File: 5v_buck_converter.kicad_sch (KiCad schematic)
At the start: 0 parts

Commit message: Finished 5V buck converter schematic
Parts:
- added C15, C20, C22: 22uF, symbol Device:C
- added C16, C17, C21: 10uF, symbol Device:C
- added C18: 0.1uF, symbol Device:C
- added C19: 0.1uF, symbol Device:C_Small
- added IC2: TPS62933ODRLR, SOTFL50P160X60-8N, symbol utsvt-chips:TPS62933ODRLR
- added L2: 6.6uH, symbol Device:L
- added Q6: BUK9K52-60RAX, symbol Device:Q_Dual_NMOS_S1G1S2G2D2D2D1D1
- added R27: 1.5k, symbol Device:R_Small
- added R28: 10k, symbol Device:R_Small
- added R30: 51k, symbol Device:R_Small
- added R31: 200k, symbol Device:R_Small
- added R33: 18k, symbol Device:R_Small
- added R34: 360, symbol Device:R_Small
- added R35: 10k, symbol Device:R
- added R36: 1k, symbol Device:R
- added R4: 5, symbol Device:R_Small
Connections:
- new net: IC2.2 (EN), R31.2, R33.1
- new net: R33.2, R34.1
- new net: Q6.2 (G), Q6.4 (G), R35.2, R36.2
- new net: C19.1, IC2.5 (SW), L2.1
- new net: C19.2, R4.2
- new net: IC2.6 (BST), R4.1
- new net: R27.1, R30.2
- new net: IC2.8 (FB), R27.2, R28.1
- new net: Q6.1 (S), Q6.3 (S)
- new net +3.3V: R35.1
- new net 5V_OUT: Q6.5 (D), Q6.6 (D)
- new net GND: C15.1, C16.2, C17.2, C18.2, C20.1, C21.1, C22.1, IC2.4 (GND), R28.2, R34.2
- new net POWER_GOOD: IC2.7 (PG), R36.1
- new net VBUS_IN: C16.1, C17.1, C18.1, IC2.3 (VIN), R31.1
- new net VOUT: C15.2, C20.2, C21.2, C22.2, L2.2, Q6.7 (D), Q6.8 (D), R30.1
- no-connect marks 0 -> 1
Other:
- note added: "3.3V from internal regulator of PD controller"
- note added: "500kHz See datasheet pg. 20"
- note added: "5V Buck"
- note added: "Note: test performance of this output filter to ensure capacitance is not too high. Remove capacitors if necessary."
- note added: "Output MOSFET (N-Channel)"
- note added: "Output Voltage = 5V See datasheet pg. 19"
- note added: "Undervoltage Lockout Settings: Vstart = 14.25V Vstop = 13.5V See datasheet pg. 21"
- company: (none) -> Longhorn Racing Solar

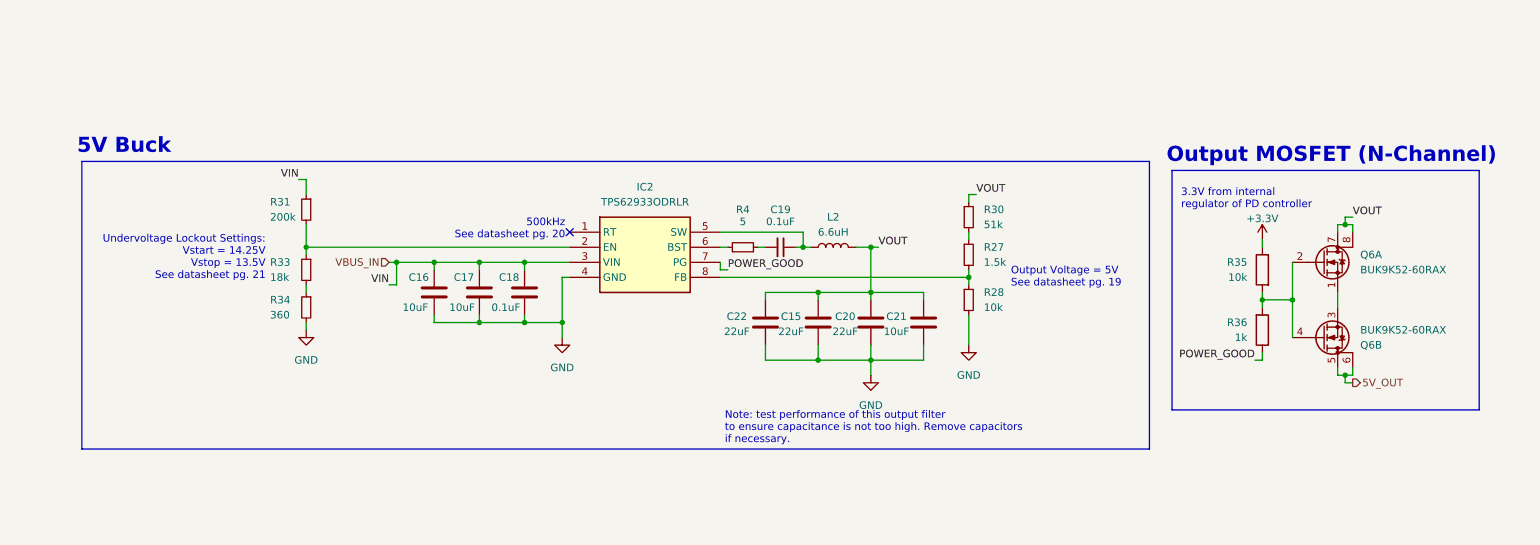
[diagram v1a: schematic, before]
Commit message: added power good LED indicators
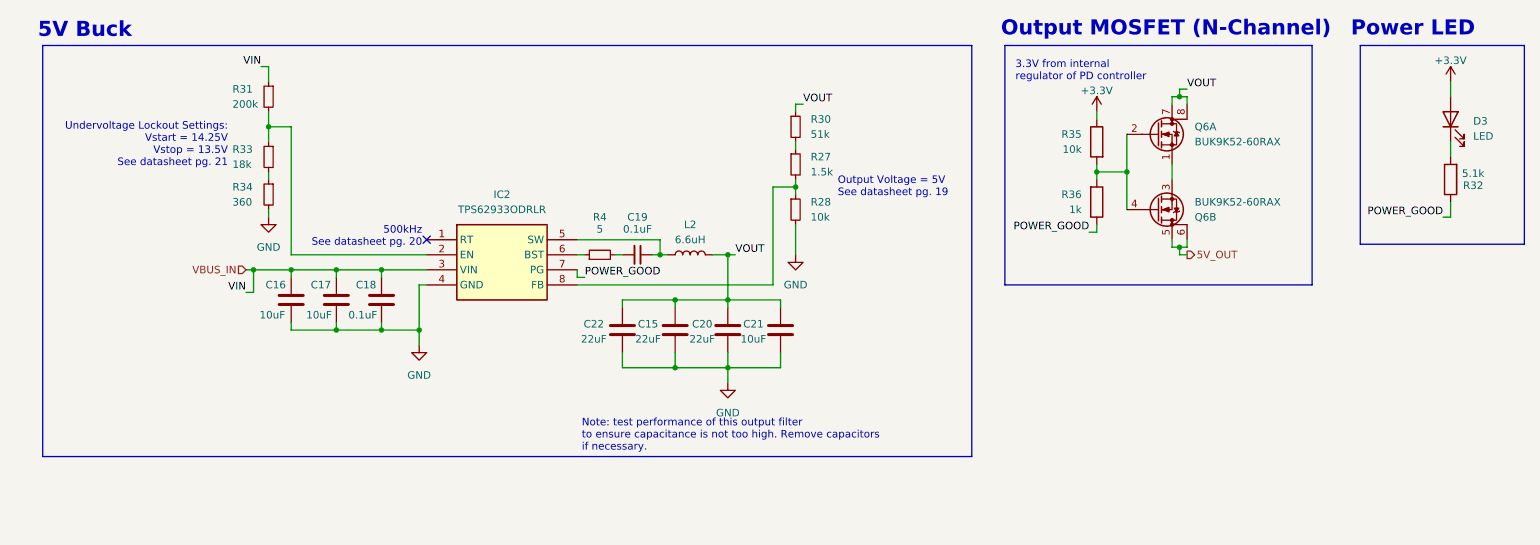
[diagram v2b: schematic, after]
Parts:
- added D3: LED, symbol Device:LED
- added R32: 5.1k, symbol Device:R
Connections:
- net +3.3V: now also D3.2 (A)
- net POWER_GOOD: now also R32.1
- new net: D3.1 (K), R32.2
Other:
- note added: "Power LED"
- moved on the sheet: C15, C16, C17, C18, C19, C20, C21, C22, IC2, L2, Q6A, Q6B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

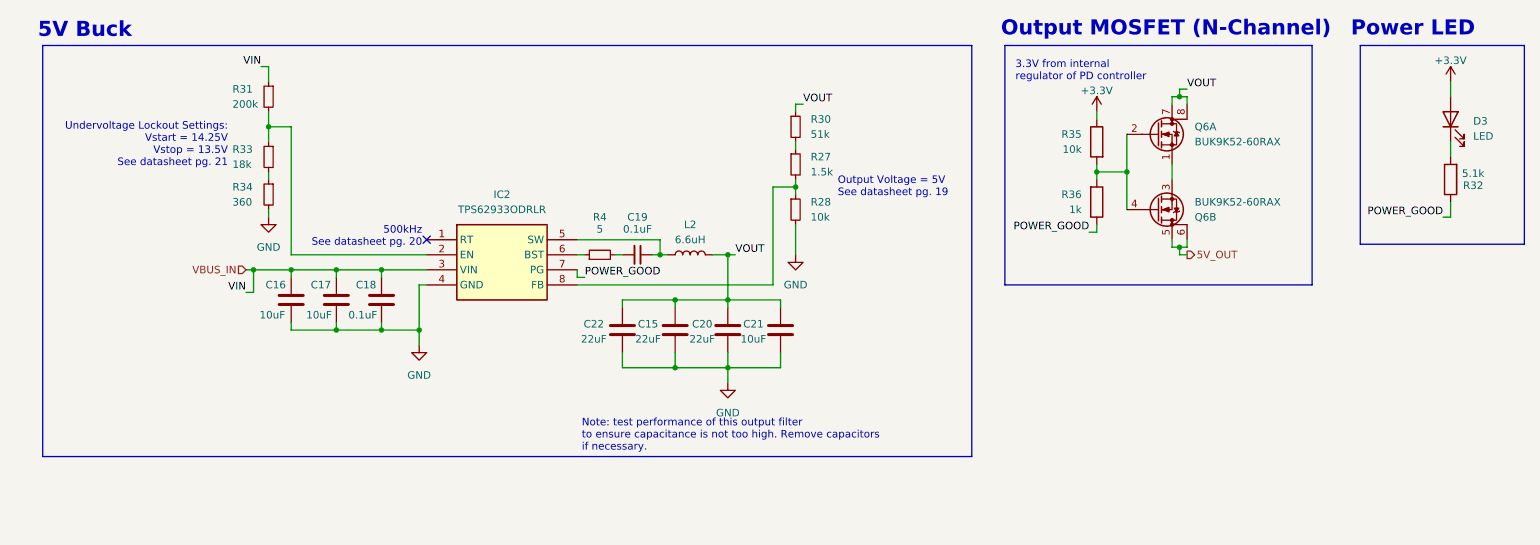
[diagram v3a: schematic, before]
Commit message: updated with some new footprints (have yet to finish footprint assignment; also need to switch out inductor for 5V buck)
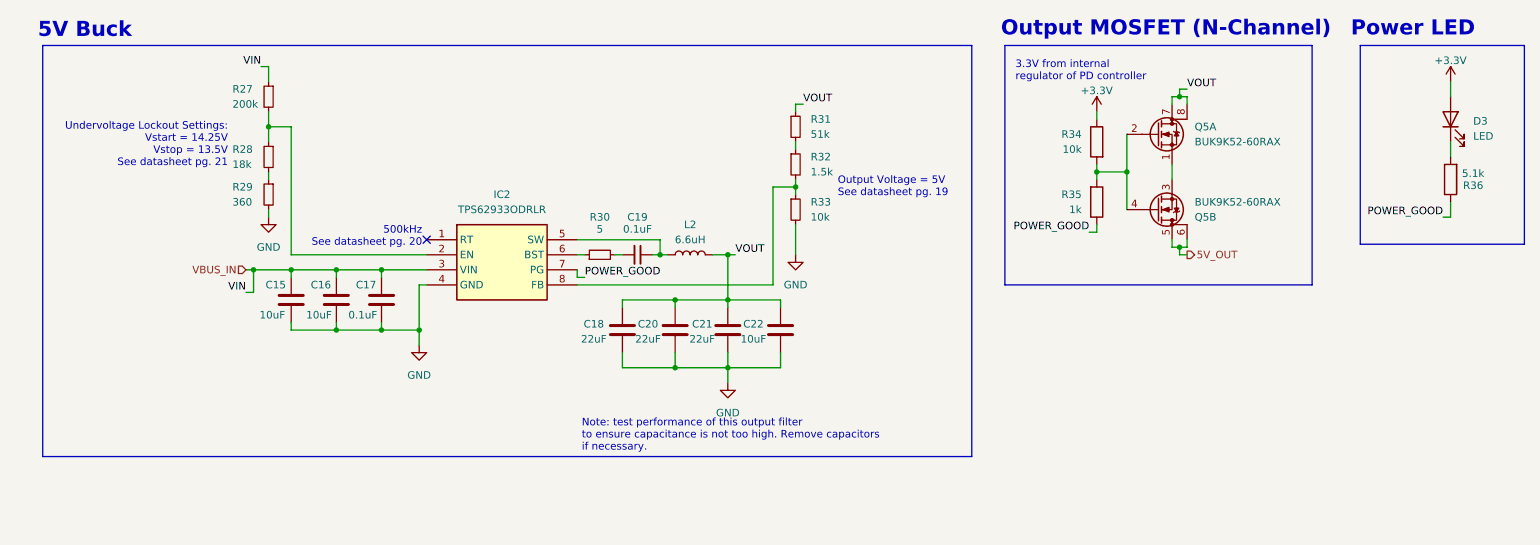
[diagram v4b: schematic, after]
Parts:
- C15: renamed from C16; footprint (none) -> Capacitor_SMD:C_0805_2012Metric
- C16: renamed from C17; footprint (none) -> Capacitor_SMD:C_0805_2012Metric
- C17: renamed from C18; footprint (none) -> Capacitor_SMD:C_0805_2012Metric
- C18: renamed from C22; footprint (none) -> Capacitor_SMD:C_0805_2012Metric
- C19: footprint (none) -> Capacitor_SMD:C_0805_2012Metric
- C20: renamed from C15; footprint (none) -> Capacitor_SMD:C_0805_2012Metric
- C21: renamed from C20; footprint (none) -> Capacitor_SMD:C_0805_2012Metric
- C22: renamed from C21; footprint (none) -> Capacitor_SMD:C_0805_2012Metric
- IC2: footprint SOTFL50P160X60-8N -> UTSVT_Power:SOTFL50P160X60-8N; symbol utsvt-chips:TPS62933ODRLR -> utsvt-power-regulators:TPS62933ODRLR
- R27: renamed from R31; footprint (none) -> Resistor_SMD:R_0805_2012Metric
- R28: renamed from R33; footprint (none) -> Resistor_SMD:R_0805_2012Metric
- R29: renamed from R34; footprint (none) -> Resistor_SMD:R_0805_2012Metric
- R30: renamed from R4; footprint (none) -> Resistor_SMD:R_0805_2012Metric
- R31: renamed from R30; footprint (none) -> Resistor_SMD:R_0805_2012Metric
- R32: renamed from R27; footprint (none) -> Resistor_SMD:R_0805_2012Metric
- R33: renamed from R28; footprint (none) -> Resistor_SMD:R_0805_2012Metric
- R34: renamed from R35; footprint (none) -> Resistor_SMD:R_0805_2012Metric
- R35: renamed from R36; footprint (none) -> Resistor_SMD:R_0805_2012Metric
- R36: renamed from R32; footprint (none) -> Resistor_SMD:R_0805_2012Metric
- renumbered Q6 to Q5

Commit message: changed 5v buck to TPS56A37
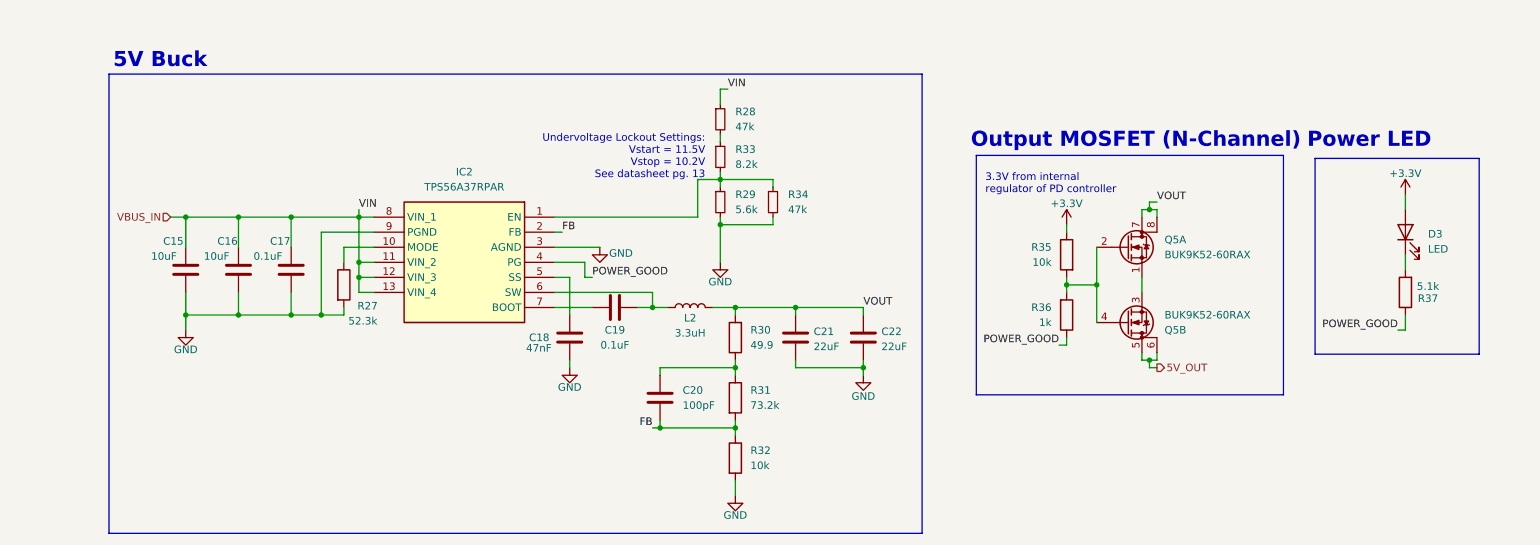
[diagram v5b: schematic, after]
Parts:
- removed C19: 0.1uF, Capacitor_SMD:C_0805_2012Metric, symbol Device:C_Small
- removed IC2: TPS62933ODRLR, UTSVT_Power:SOTFL50P160X60-8N, symbol utsvt-power-regulators:TPS62933ODRLR
- removed R27: 200k, Resistor_SMD:R_0805_2012Metric, symbol Device:R_Small
- removed R30: 5, Resistor_SMD:R_0805_2012Metric, symbol Device:R_Small
- removed R31: 51k, Resistor_SMD:R_0805_2012Metric, symbol Device:R_Small
- removed R32: 1.5k, Resistor_SMD:R_0805_2012Metric, symbol Device:R_Small
- removed R34: 10k, Resistor_SMD:R_0805_2012Metric, symbol Device:R
- added C19: 0.1uF, Capacitor_SMD:C_0805_2012Metric, symbol Device:C
- added IC2: TPS56A37RPAR, UTSVT_Power:TPS56A37RPAR, symbol utsvt-power-regulators:TPS56A37RPAR
- added R27: 52.3k, Resistor_SMD:R_0805_2012Metric, symbol Device:R
- added R30: 49.9, Resistor_SMD:R_0805_2012Metric, symbol Device:R
- added R31: 73.2k, Resistor_SMD:R_0805_2012Metric, symbol Device:R
- added R32: 10k, Resistor_SMD:R_0805_2012Metric, symbol Device:R
- added R34: 47k, Resistor_SMD:R_0805_2012Metric, symbol Device:R_Small
- added R37: 5.1k, Resistor_SMD:R_0805_2012Metric, symbol Device:R
- C18: value 22uF -> 47nF
- C20: value 22uF -> 100pF
- C22: value 10uF -> 22uF
- L2: value 6.6uH -> 3.3uH; footprint (none) -> UTSVT_Passive:INDPM135125X640N; Mouser Part Number (none) -> SRP1265A-5R6M
- R28: value 18k -> 47k
- R29: value 360 -> 5.6k
- R33: value 10k -> 8.2k
- R35: value 1k -> 10k
- R36: value 5.1k -> 1k
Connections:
- net +3.3V: now also R35.1
- net GND: now also C18.2, C21.2, C22.2, IC2.3 (AGND), IC2.9 (PGND), R27.2, R32.2, R34.2; no longer C18.1, C20.1, C21.1, C22.1, R33.2
- net POWER_GOOD: now also IC2.4 (PG), R37.1; no longer R35.1
- net VBUS_IN: now also R28.1, IC2.11 (VIN_2), IC2.12 (VIN_3), IC2.13 (VIN_4), IC2.8 (VIN_1)
- net VOUT: now also C21.1, C22.1, R30.2; no longer C18.2, C20.2, C21.2, C22.2
- net at R28.2: now also R33.1; no longer R29.1
- net at Q5.2 (G), Q5.4 (G), R35.2: now also R36.2
- net at L2.1: now also C19.2, IC2.6 (SW)
- net at D3.1 (K): now also R37.2; no longer R36.2
- new net: C18.1, IC2.5 (SS)
- new net: C20.1, R30.1, R31.1
- new net: IC2.10 (MODE), R27.1
- new net: IC2.1 (EN), R29.1, R33.2, R34.1
- new net: C19.1, IC2.7 (BOOT)
- new net FB: C20.2, IC2.2 (FB), R31.2, R32.1
- no-connect marks 1 -> 0
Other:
- note added: "Undervoltage Lockout Settings: Vstart = 11.5V Vstop = 10.2V See datasheet pg. 13"
- note removed: "500kHz See datasheet pg. 20"
- note removed: "Note: test performance of this output filter to ensure capacitance is not too high. Remove capacitors if necessary."
- note removed: "Output Voltage = 5V See datasheet pg. 19"
- note removed: "Undervoltage Lockout Settings: Vstart = 14.25V Vstop = 13.5V See datasheet pg. 21"

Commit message: almost done w/ schematic, just need to finish footprint assignment (make sure buck converter components are correctly chosen and there aren't caps that need to be different and stuff)
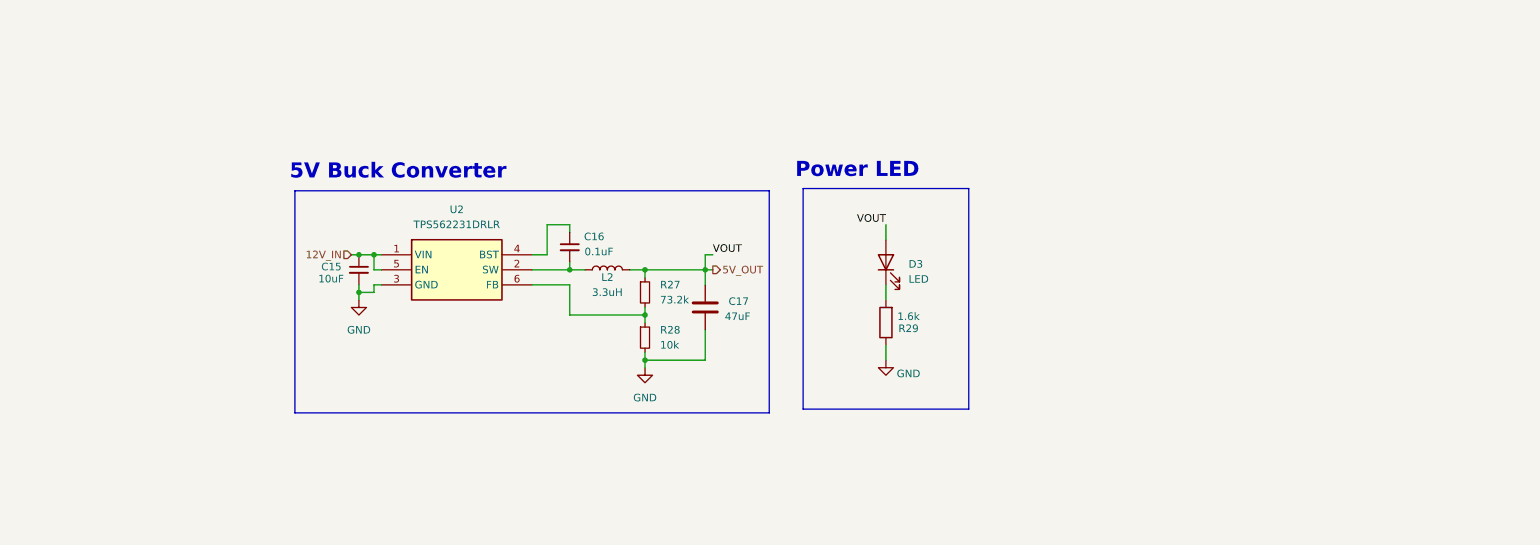
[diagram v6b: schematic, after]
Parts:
- removed C15, C16: 10uF, Capacitor_SMD:C_0805_2012Metric, symbol Device:C
- removed C18: 47nF, Capacitor_SMD:C_0805_2012Metric, symbol Device:C
- removed C19: 0.1uF, Capacitor_SMD:C_0805_2012Metric, symbol Device:C
- removed C20: 100pF, Capacitor_SMD:C_0805_2012Metric, symbol Device:C
- removed C21, C22: 22uF, Capacitor_SMD:C_0805_2012Metric, symbol Device:C
- removed IC2: TPS56A37RPAR, UTSVT_Power:TPS56A37RPAR, symbol utsvt-power-regulators:TPS56A37RPAR
- removed Q5: BUK9K52-60RAX, symbol Device:Q_Dual_NMOS_S1G1S2G2D2D2D1D1
- removed R27: 52.3k, Resistor_SMD:R_0805_2012Metric, symbol Device:R
- removed R29: 5.6k, Resistor_SMD:R_0805_2012Metric, symbol Device:R_Small
- removed R30: 49.9, Resistor_SMD:R_0805_2012Metric, symbol Device:R
- removed R31: 73.2k, Resistor_SMD:R_0805_2012Metric, symbol Device:R
- removed R32, R35: 10k, Resistor_SMD:R_0805_2012Metric, symbol Device:R
- removed R33: 8.2k, Resistor_SMD:R_0805_2012Metric, symbol Device:R_Small
- removed R34: 47k, Resistor_SMD:R_0805_2012Metric, symbol Device:R_Small
- removed R36: 1k, Resistor_SMD:R_0805_2012Metric, symbol Device:R
- added C15: 10uF, Capacitor_SMD:C_0805_2012Metric, symbol Device:C_Small
- added C16: 0.1uF, Capacitor_SMD:C_0805_2012Metric, symbol Device:C_Small
- added R27: 73.2k, symbol Device:R_Small
- added U2: TPS562231DRLR, Package_TO_SOT_SMD:SOT-563, symbol utsvt-power-regulators:TPS562231DRLR
- C17: value 0.1uF -> 47uF
- D3: footprint (none) -> LED_SMD:LED_0805_2012Metric; Mouser Part Number (none) -> APTD2012LCGCK
- L2: footprint UTSVT_Passive:INDPM135125X640N -> (none); Mouser Part Number SRP1265A-5R6M -> LBC3225T3R3MR
- R28: value 47k -> 10k; footprint Resistor_SMD:R_0805_2012Metric -> (none)
- R29: renamed from R37; value 5.1k -> 1.6k
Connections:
- net +3.3V is gone; now on net 5V_OUT: D3.2 (A)
- net POWER_GOOD is gone; now on net GND: R29.1
- net VOUT is gone; now on net 5V_OUT: L2.2
- net 5V_OUT: now also C17.1, R27.1
- net GND: now also R28.2, C15.2, U2.3 (GND)
- net at L2.1: now also C16.2, U2.2 (SW)
- net VBUS_IN: no longer names the net of R28.1
- net VBUS_IN: now also R27.2, U2.6 (FB); no longer C17.1
- new net: C16.1, U2.4 (BST)
- new net 12V_IN: C15.1, U2.1 (VIN), U2.5 (EN)
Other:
- note added: "5V Buck Converter"
- note removed: "3.3V from internal regulator of PD controller"
- note removed: "5V Buck"
- note removed: "Output MOSFET (N-Channel)"
- note removed: "Undervoltage Lockout Settings: Vstart = 11.5V Vstop = 10.2V See datasheet pg. 13"
- moved on the sheet: D3, R29

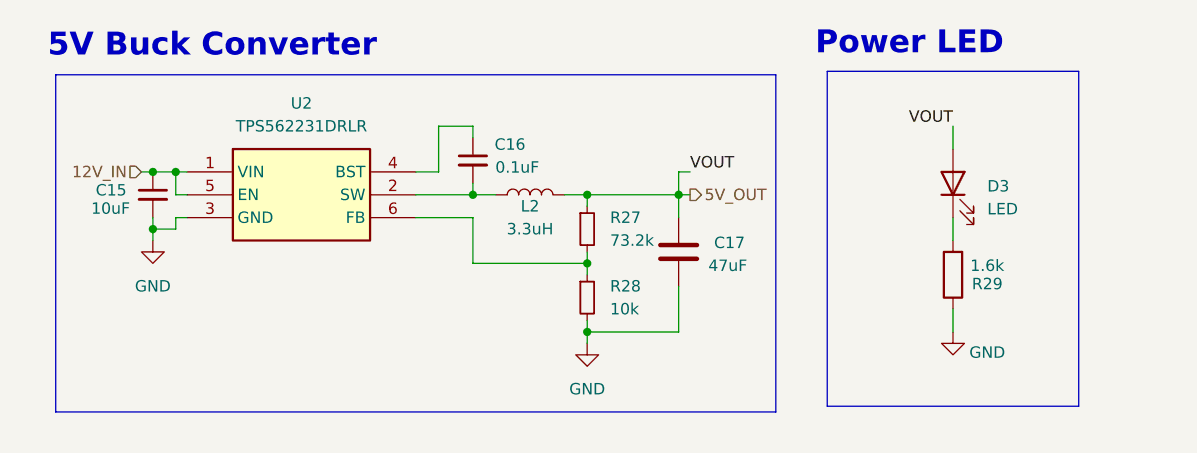
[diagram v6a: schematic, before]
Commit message: cleaned up schematic, added power LEDs and testpoints
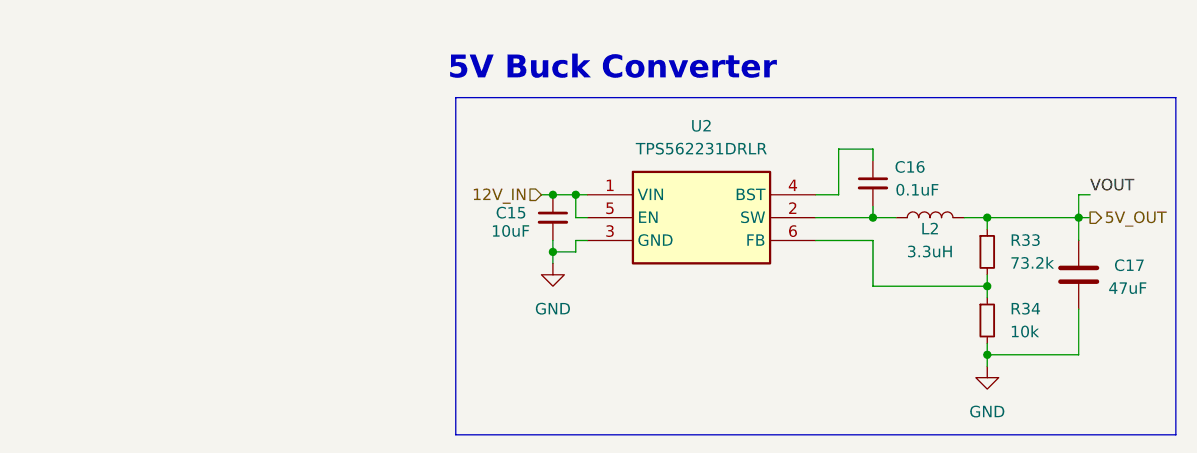
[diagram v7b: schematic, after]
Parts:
- removed D3: LED, LED_SMD:LED_0805_2012Metric, symbol Device:LED
- removed R29: 1.6k, Resistor_SMD:R_0805_2012Metric, symbol Device:R
- renumbered R27 to R33, R28 to R34
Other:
- note removed: "Power LED"
- moved on the sheet: C15, C16, C17, L2, R33, R34, U2

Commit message: finished footprint assignment
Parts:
- L2: footprint (none) -> Capacitor_SMD:C_1210_3225Metric
- R33, R34: footprint (none) -> Resistor_SMD:R_0805_2012Metric
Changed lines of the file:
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@@
 			)
 		)
-		(property "Footprint" ""
+		(property "Footprint" "Resistor_SMD:R_0805_2012Metric"
 			(at 166.37 101.6 0)
 			(effects
@@
 			)
 		)
-		(property "Footprint" ""
+		(property "Footprint" "Resistor_SMD:R_0805_2012Metric"
 			(at 166.37 109.22 0)
 			(effects
@@
 			)
 		)
-		(property "Footprint" ""
+		(property "Footprint" "Capacitor_SMD:C_1210_3225Metric"
 			(at 160.02 97.79 0)
 			(effects
